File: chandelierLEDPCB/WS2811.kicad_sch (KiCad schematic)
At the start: 14 parts, among them Q1 Si2301CDS, Q2 Si2301CDS, Q3 Si2301CDS, U1 WS2811

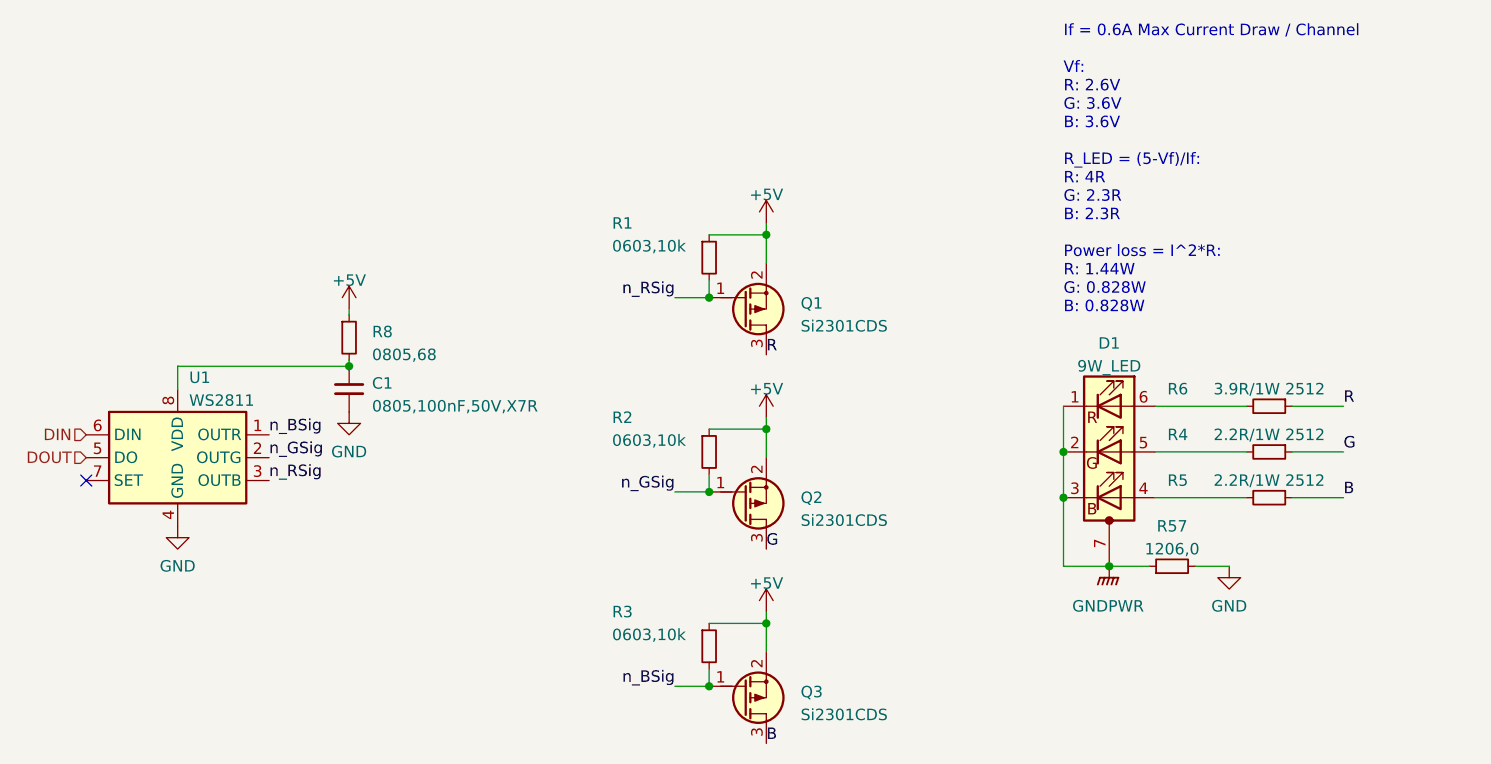
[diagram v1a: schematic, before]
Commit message: Edited LED to have EP disconnected
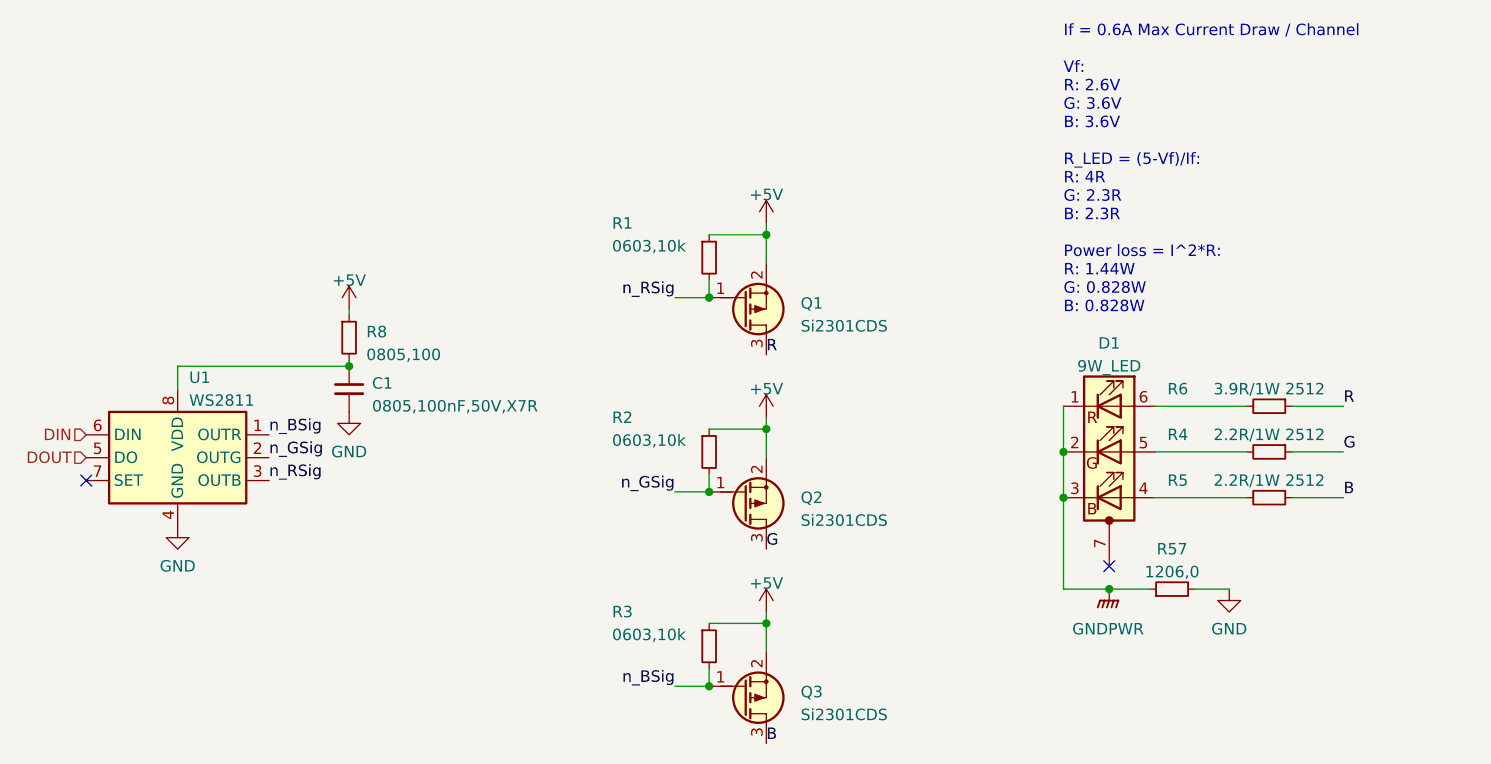
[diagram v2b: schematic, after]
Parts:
- R8: value 0805,68 -> 0805,100
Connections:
- net GNDPWR: no longer D1.7 (PAD)
- no-connect marks 1 -> 2
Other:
- moved on the sheet: R57
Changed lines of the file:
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@@
   (paper "USLetter")
   (title_block
-    (date "2023-04-08")
-    (rev "A01")
-  )
-  (junction (at 180.34 111.125) (diameter 0) (color 0 0 0 0)
+    (date "2023-04-24")
+    (rev "B01")
   )
   (junction (at 135.89 81.28) (diameter 0) (color 0 0 0 0)
@@
   (junction (at 142.24 74.295) (diameter 0) (color 0 0 0 0)
   )
+  (junction (at 180.34 113.665) (diameter 0) (color 0 0 0 0)
+  )
   (junction (at 135.89 124.46) (diameter 0) (color 0 0 0 0)
   )
@@
   (junction (at 175.26 98.425) (diameter 0) (color 0 0 0 0)
   )
+  (no_connect (at 180.34 111.125))
   (no_connect (at 66.675 101.6))
   (wire (pts (xy 135.89 100.965) (xy 135.89 102.87))
@@
     (stroke (width 0) (type default))
   )
+  (wire (pts (xy 189.865 113.665) (xy 193.675 113.665))
+    (stroke (width 0) (type default))
+  )
   (wire (pts (xy 132.08 124.46) (xy 135.89 124.46))
     (stroke (width 0) (type default))
@@
     (stroke (width 0) (type default))
   )
-  (wire (pts (xy 180.34 111.125) (xy 175.26 111.125))
-    (stroke (width 0) (type default))
-  )
-  (wire (pts (xy 175.26 103.505) (xy 175.26 111.125))
+  (wire (pts (xy 180.34 113.665) (xy 175.26 113.665))
+    (stroke (width 0) (type default))
+  )
+  (wire (pts (xy 175.26 103.505) (xy 175.26 113.665))
     (stroke (width 0) (type default))
   )
@@
     (stroke (width 0) (type default))
   )
-  (wire (pts (xy 180.34 111.125) (xy 184.785 111.125))
+  (wire (pts (xy 180.34 113.665) (xy 184.785 113.665))
     (stroke (width 0) (type default))
   )
@@
   )
   (wire (pts (xy 185.42 98.425) (xy 195.58 98.425))
-    (stroke (width 0) (type default))
-  )
-  (wire (pts (xy 189.865 111.125) (xy 193.675 111.125))
     (stroke (width 0) (type default))
   )
@@
   (symbol (lib_id "jlcpcb-basic-resistor:0805,68") (at 95.885 85.725 0) (unit 1)
     (in_bom yes) (on_board yes) (dnp no) (fields_autoplaced)
-    (property "Reference" "R8" (at 98.425 85.09 0)
-      (effects (font (size 1.27 1.27)) (justify left))
-    )
-    (property "Value" "0805,68" (at 98.425 87.63 0)
+    (property "Reference" "R8" (at 97.79 85.09 0)
+      (effects (font (size 1.27 1.27)) (justify left))
+    )
+    (property "Value" "0805,100" (at 97.79 87.63 0)
       (effects (font (size 1.27 1.27)) (justify left))
     )
@@
     )
   )
-  (symbol (lib_id "jlcpcb-basic-resistor:1206,0") (at 187.325 111.125 90) (unit 1)
-    (in_bom yes) (on_board yes) (dnp no) (fields_autoplaced)
-    (property "Reference" "R57" (at 187.325 106.68 90)
-      (effects (font (size 1.27 1.27)))
-    )
-    (property "Value" "1206,0" (at 187.325 109.22 90)
-      (effects (font (size 1.27 1.27)))
-    )
-    (property "Footprint" "R_1206_3216Metric" (at 187.325 111.125 0)
-      (effects (font (size 1.27 1.27)) hide)
-    )
-    (property "Datasheet" "https://datasheet.lcsc.com/lcsc/2110251930_UNI-ROYAL-Uniroyal-Elec-1206W4F0000T5E_C17888.pdf" (at 187.325 111.125 0)
-      (effects (font (size 1.27 1.27)) hide)
-    )
-    (property "LCSC" "C17888" (at 187.325 111.125 0)
-      (effects (font (size 0 0)) hide)
-    )
-    (property "MFG" "UNI-ROYAL(Uniroyal Elec)" (at 187.325 111.125 0)
-      (effects (font (size 0 0)) hide)
-    )
-    (property "MFGPN" "1206W4F0000T5E" (at 187.325 111.125 0)
+  (symbol (lib_id "jlcpcb-basic-resistor:1206,0") (at 187.325 113.665 90) (unit 1)
+    (in_bom yes) (on_board yes) (dnp no) (fields_autoplaced)
+    (property "Reference" "R57" (at 187.325 109.22 90)
+      (effects (font (size 1.27 1.27)))
+    )
+    (property "Value" "1206,0" (at 187.325 111.76 90)
+      (effects (font (size 1.27 1.27)))
+    )
+    (property "Footprint" "R_1206_3216Metric" (at 187.325 113.665 0)
+      (effects (font (size 1.27 1.27)) hide)
+    )
+    (property "Datasheet" "https://datasheet.lcsc.com/lcsc/2110251930_UNI-ROYAL-Uniroyal-Elec-1206W4F0000T5E_C17888.pdf" (at 187.325 113.665 0)
+      (effects (font (size 1.27 1.27)) hide)
+    )
+    (property "LCSC" "C17888" (at 187.325 113.665 0)
+      (effects (font (size 0 0)) hide)
+    )
+    (property "MFG" "UNI-ROYAL(Uniroyal Elec)" (at 187.325 113.665 0)
+      (effects (font (size 0 0)) hide)
+    )
+    (property "MFGPN" "1206W4F0000T5E" (at 187.325 113.665 0)
       (effects (font (size 0 0)) hide)
     )
@@
     )
   )
-  (symbol (lib_id "power:GNDPWR") (at 180.34 111.125 0) (unit 1)
-    (in_bom yes) (on_board yes) (dnp no) (fields_autoplaced)
-    (property "Reference" "#PWR06" (at 180.34 116.205 0)
-      (effects (font (size 1.27 1.27)) hide)
-    )
-    (property "Value" "GNDPWR" (at 180.213 115.57 0)
-      (effects (font (size 1.27 1.27)))
-    )
-    (property "Footprint" "" (at 180.34 112.395 0)
-      (effects (font (size 1.27 1.27)) hide)
-    )
-    (property "Datasheet" "" (at 180.34 112.395 0)
+  (symbol (lib_id "power:GNDPWR") (at 180.34 113.665 0) (unit 1)
+    (in_bom yes) (on_board yes) (dnp no) (fields_autoplaced)
+    (property "Reference" "#PWR06" (at 180.34 118.745 0)
+      (effects (font (size 1.27 1.27)) hide)
+    )
+    (property "Value" "GNDPWR" (at 180.213 118.11 0)
+      (effects (font (size 1.27 1.27)))
+    )
+    (property "Footprint" "" (at 180.34 114.935 0)
+      (effects (font (size 1.27 1.27)) hide)
+    )
+    (property "Datasheet" "" (at 180.34 114.935 0)
       (effects (font (size 1.27 1.27)) hide)
     )
@@
     )
   )
-  (symbol (lib_id "power:GND") (at 193.675 111.125 0) (unit 1)
-    (in_bom yes) (on_board yes) (dnp no) (fields_autoplaced)
-    (property "Reference" "#PWR057" (at 193.675 117.475 0)
-      (effects (font (size 1.27 1.27)) hide)
-    )
-    (property "Value" "GND" (at 193.675 115.57 0)
-      (effects (font (size 1.27 1.27)))
-    )
-    (property "Footprint" "" (at 193.675 111.125 0)
-      (effects (font (size 1.27 1.27)) hide)
-    )
-    (property "Datasheet" "" (at 193.675 111.125 0)
-      (effects (font (size 1.27 1.27)) hide)
-    )
+  (symbol (lib_id "power:GND") (at 193.675 113.665 0) (unit 1)
+    (in_bom yes) (on_board yes) (dnp no) (fields_autoplaced)
+    (property "Reference" "#PWR057" (at 193.675 120.015 0)
+      (effects (font (size 1.27 1.27)) hide)
+    )
+    (property "Value" "GND" (at 193.675 118.11 0)
+      (effects (font (size 1.27 1.27)))
+    )
+    (property "Footprint" "" (at 193.675 113.665 0)
+      (effects (font (size 1.27 1.27)) hide)
+    )
+    (property "Datasheet" "" (at 193.675 113.665 0)
+      (effects (font (size 1.27 1.27)) hide)
+    )
